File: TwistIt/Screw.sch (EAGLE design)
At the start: 7 parts

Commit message: Brush up twistit
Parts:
- removed U$3: (no value), pie:POGO_PIN
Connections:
- net PIN2 renamed P2
- removed net PIN1: R3.1, U$1.A0, U$2.P$2
- removed net PIN3: R1.1, U$1.A2, U$2.P$4
- new net P1: R1.1, U$1.A2, U$2.P$2
- new net P3: R3.1, U$1.A0, U$2.P$4
- net GND: now also U$2.P$5; no longer U$2.P$1
- net VCC: now also U$2.P$1; no longer U$2.P$5
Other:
- note removed: "PIN1"
- note removed: "PIN2"
- note removed: "PIN3"
- note removed: "Pin 1"
- note removed: "Pin 2"
- note removed: "Pin 3"
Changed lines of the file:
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@@
 <part name="R2" library="resistor" deviceset="R-US_" device="R0603"/>
 <part name="R3" library="resistor" deviceset="R-US_" device="R0603"/>
-<part name="SUPPLY1" library="pie" deviceset="GND" device=""/>
 <part name="SUPPLY2" library="pie" deviceset="GND" device=""/>
 <part name="JP1" library="jumper" deviceset="JP1E" device=""/>
 <part name="U$2" library="pie" deviceset="5PIN_SCREW" device=""/>
-<part name="U$3" library="pie" deviceset="POGO_PIN" device=""/>
+<part name="SUPPLY1" library="pie" deviceset="GND" device=""/>
 </parts>
 <sheets>
 <sheet>
 <plain>
-<text x="134.62" y="114.3" size="1.778" layer="91">Pin 1</text>
-<text x="127" y="114.3" size="1.778" layer="91">Pin 2</text>
-<text x="119.38" y="114.3" size="1.778" layer="91">Pin 3</text>
-<text x="83.82" y="88.9" size="1.778" layer="91">PIN1</text>
-<text x="83.82" y="91.44" size="1.778" layer="91">PIN2</text>
-<text x="83.82" y="93.98" size="1.778" layer="91">PIN3</text>
 </plain>
 <instances>
@@
 <instance part="R2" gate="G$1" x="116.84" y="99.06" rot="R180"/>
 <instance part="R3" gate="G$1" x="116.84" y="93.98" rot="R180"/>
-<instance part="SUPPLY1" gate="GND" x="134.62" y="81.28"/>
 <instance part="SUPPLY2" gate="GND" x="27.94" y="99.06"/>
 <instance part="JP1" gate="A" x="93.98" y="101.6"/>
-<instance part="U$2" gate="G$1" x="152.4" y="96.52"/>
-<instance part="U$3" gate="G$1" x="170.18" y="116.84"/>
+<instance part="U$2" gate="G$1" x="101.6" y="71.12" rot="R180"/>
+<instance part="SUPPLY1" gate="GND" x="124.46" y="55.88"/>
 </instances>
 <busses>
@@
 </segment>
 <segment>
-<wire x1="134.62" y1="88.9" x2="134.62" y2="83.82" width="0.1524" layer="91"/>
+<pinref part="U$2" gate="G$1" pin="P$5"/>
+<wire x1="116.84" y1="58.42" x2="124.46" y2="58.42" width="0.1524" layer="91"/>
 <pinref part="SUPPLY1" gate="GND" pin="GND"/>
-<pinref part="U$2" gate="G$1" pin="P$1"/>
-<wire x1="134.62" y1="88.9" x2="137.16" y2="88.9" width="0.1524" layer="91"/>
-<junction x="137.16" y="88.9"/>
+</segment>
+</net>
+<net name="P1" class="0">
+<segment>
+<pinref part="R1" gate="G$1" pin="1"/>
+<wire x1="121.92" y1="104.14" x2="129.54" y2="104.14" width="0.1524" layer="91"/>
+</segment>
+<segment>
+<pinref part="U$2" gate="G$1" pin="P$2"/>
+<wire x1="116.84" y1="73.66" x2="124.46" y2="73.66" width="0.1524" layer="91"/>
+<label x="121.92" y="73.66" size="1.778" layer="95"/>
+</segment>
+<segment>
+<pinref part="U$1" gate="G$1" pin="A2"/>
+<wire x1="76.2" y1="93.98" x2="83.82" y2="93.98" width="0.1524" layer="91"/>
 </segment>
 </net>
 <net name="VCC" class="0">
 <segment>
+<pinref part="U$2" gate="G$1" pin="P$1"/>
+<wire x1="116.84" y1="78.74" x2="124.46" y2="78.74" width="0.1524" layer="91"/>
+<label x="121.92" y="78.74" size="1.778" layer="95"/>
+</segment>
+<segment>
 <pinref part="JP1" gate="A" pin="1"/>
 <pinref part="U$1" gate="G$1" pin="VCC"/>
-<wire x1="76.2" y1="99.06" x2="86.36" y2="99.06" width="0.1524" layer="91"/>
-<wire x1="86.36" y1="99.06" x2="93.98" y2="99.06" width="0.1524" layer="91"/>
-<wire x1="86.36" y1="99.06" x2="86.36" y2="109.22" width="0.1524" layer="91"/>
-<junction x="86.36" y="99.06"/>
-<pinref part="U$2" gate="G$1" pin="P$5"/>
-<wire x1="86.36" y1="109.22" x2="137.16" y2="109.22" width="0.1524" layer="91"/>
-<junction x="137.16" y="109.22"/>
+<wire x1="76.2" y1="99.06" x2="93.98" y2="99.06" width="0.1524" layer="91"/>
 </segment>
 </net>
-<net name="PIN1" class="0">
+<net name="P2" class="0">
+<segment>
+<pinref part="U$2" gate="G$1" pin="P$3"/>
+<wire x1="116.84" y1="68.58" x2="124.46" y2="68.58" width="0.1524" layer="91"/>
+<label x="121.92" y="68.58" size="1.778" layer="95"/>
+</segment>
+<segment>
+<pinref part="U$1" gate="G$1" pin="A1"/>
+<wire x1="76.2" y1="91.44" x2="83.82" y2="91.44" width="0.1524" layer="91"/>
+</segment>
+<segment>
+<pinref part="R2" gate="G$1" pin="1"/>
+<wire x1="121.92" y1="99.06" x2="129.54" y2="99.06" width="0.1524" layer="91"/>
+</segment>
+</net>
+<net name="P3" class="0">
+<segment>
+<pinref part="U$2" gate="G$1" pin="P$4"/>
+<wire x1="116.84" y1="63.5" x2="124.46" y2="63.5" width="0.1524" layer="91"/>
+<label x="121.92" y="63.5" size="1.778" layer="95"/>
+</segment>
 <segment>
 <pinref part="U$1" gate="G$1" pin="A0"/>
@@
 <segment>
 <pinref part="R3" gate="G$1" pin="1"/>
-<wire x1="121.92" y1="93.98" x2="124.46" y2="93.98" width="0.1524" layer="91"/>
-<wire x1="124.46" y1="93.98" x2="124.46" y2="111.76" width="0.1524" layer="91"/>
-<pinref part="U$2" gate="G$1" pin="P$2"/>
-<wire x1="124.46" y1="93.98" x2="137.16" y2="93.98" width="0.1524" layer="91"/>
-<junction x="124.46" y="93.98"/>
-<junction x="137.16" y="93.98"/>
+<wire x1="121.92" y1="93.98" x2="129.54" y2="93.98" width="0.1524" layer="91"/>
 </segment>
 </net>
-<net name="PIN2" class="0">
-<segment>
-<pinref part="R2" gate="G$1" pin="1"/>
-<wire x1="121.92" y1="99.06" x2="129.54" y2="99.06" width="0.1524" layer="91"/>
-<wire x1="129.54" y1="99.06" x2="137.16" y2="99.06" width="0.1524" layer="91"/>
-<wire x1="137.16" y1="99.06" x2="138.43" y2="99.06" width="0.1524" layer="91"/>
-<wire x1="129.54" y1="99.06" x2="129.54" y2="111.76" width="0.1524" layer="91"/>
-<junction x="129.54" y="99.06"/>
-<pinref part="U$2" gate="G$1" pin="P$3"/>
-<junction x="137.16" y="99.06"/>
-</segment>
-<segment>
-<pinref part="U$1" gate="G$1" pin="A1"/>
-<wire x1="76.2" y1="91.44" x2="83.82" y2="91.44" width="0.1524" layer="91"/>
-</segment>
-</net>
-<net name="PIN3" class="0">
-<segment>
-<pinref part="U$1" gate="G$1" pin="A2"/>
-<wire x1="76.2" y1="93.98" x2="83.82" y2="93.98" width="0.1524" layer="91"/>
-</segment>
-<segment>
-<pinref part="R1" gate="G$1" pin="1"/>
-<wire x1="121.92" y1="104.14" x2="134.62" y2="104.14" width="0.1524" layer="91"/>
-<wire x1="134.62" y1="104.14" x2="137.16" y2="104.14" width="0.1524" layer="91"/>
-<wire x1="137.16" y1="104.14" x2="138.43" y2="104.14" width="0.1524" layer="91"/>
-<wire x1="134.62" y1="104.14" x2="134.62" y2="111.76" width="0.1524" layer="91"/>
-<junction x="134.62" y="104.14"/>
-<pinref part="U$2" gate="G$1" pin="P$4"/>
-<junction x="137.16" y="104.14"/>
-</segment>
-</net>

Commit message: Minor fixes everywhere
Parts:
- removed U$2: 5PIN_SCREW, pie:5PIN_SCREW
- added ST1: (no value), pie:5PIN_SCREW
- R1, R2, R3: value (none) -> 330
- renumbered U$1 to APM
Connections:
- net GND: now also ST1.P$5; no longer U$2.P$5
- net P1: now also ST1.P$2; no longer U$2.P$2
- net P2: now also ST1.P$3; no longer U$2.P$3
- net P3: now also ST1.P$4; no longer U$2.P$4
- net VCC: now also ST1.P$1; no longer U$2.P$1
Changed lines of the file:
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@@
 </classes>
 <parts>
-<part name="U$1" library="pie" deviceset="ARDUINO_PRO_MICRO" device=""/>
-<part name="FRAME1" library="pie" deviceset="FRAME-LETTER" device="">
-<attribute name="REVISION" value="A"/>
+<part name="APM" library="pie" deviceset="ARDUINO_PRO_MICRO" device=""/>
+<part name="FRAME1" library="pie" deviceset="FRAME_SCHEMATIC" device="">
+<attribute name="AUTHOR" value="Mohammed Hossain, Seiya Ono"/>
+<attribute name="REVISION" value="9B"/>
 </part>
-<part name="R1" library="resistor" deviceset="R-US_" device="R0603"/>
-<part name="R2" library="resistor" deviceset="R-US_" device="R0603"/>
-<part name="R3" library="resistor" deviceset="R-US_" device="R0603"/>
+<part name="R1" library="resistor" deviceset="R-US_" device="R0603" value="330"/>
+<part name="R2" library="resistor" deviceset="R-US_" device="R0603" value="330"/>
+<part name="R3" library="resistor" deviceset="R-US_" device="R0603" value="330"/>
 <part name="SUPPLY2" library="pie" deviceset="GND" device=""/>
 <part name="JP1" library="jumper" deviceset="JP1E" device=""/>
-<part name="U$2" library="pie" deviceset="5PIN_SCREW" device=""/>
+<part name="ST1" library="pie" deviceset="5PIN_SCREW" device=""/>
 <part name="SUPPLY1" library="pie" deviceset="GND" device=""/>
 </parts>
@@
 </plain>
 <instances>
-<instance part="U$1" gate="G$1" x="60.96" y="93.98"/>
-<instance part="FRAME1" gate="G$1" x="0" y="0"/>
+<instance part="APM" gate="G$1" x="60.96" y="93.98"/>
+<instance part="FRAME1" gate="G$1" x="0" y="0">
+<attribute name="AUTHOR" x="0" y="0" size="1.778" layer="96" display="off"/>
+</instance>
 <instance part="FRAME1" gate="G$2" x="147.32" y="0">
 <attribute name="REVISION" x="147.32" y="0" size="1.778" layer="96"/>
@@
 <instance part="SUPPLY2" gate="GND" x="27.94" y="99.06"/>
 <instance part="JP1" gate="A" x="93.98" y="101.6"/>
-<instance part="U$2" gate="G$1" x="101.6" y="71.12" rot="R180"/>
+<instance part="ST1" gate="G$1" x="154.94" y="68.58"/>
 <instance part="SUPPLY1" gate="GND" x="124.46" y="55.88"/>
 </instances>
@@
 <segment>
 <pinref part="SUPPLY2" gate="GND" pin="GND"/>
-<pinref part="U$1" gate="G$1" pin="GND@0"/>
+<pinref part="APM" gate="G$1" pin="GND@0"/>
 <wire x1="27.94" y1="101.6" x2="48.26" y2="101.6" width="0.1524" layer="91"/>
 </segment>
 <segment>
-<pinref part="U$2" gate="G$1" pin="P$5"/>
-<wire x1="116.84" y1="58.42" x2="124.46" y2="58.42" width="0.1524" layer="91"/>
+<pinref part="ST1" gate="G$1" pin="P$5"/>
+<wire x1="134.62" y1="58.42" x2="124.46" y2="58.42" width="0.1524" layer="91"/>
 <pinref part="SUPPLY1" gate="GND" pin="GND"/>
 </segment>
@@
 </segment>
 <segment>
-<pinref part="U$2" gate="G$1" pin="P$2"/>
-<wire x1="116.84" y1="73.66" x2="124.46" y2="73.66" width="0.1524" layer="91"/>
+<pinref part="ST1" gate="G$1" pin="P$2"/>
+<wire x1="134.62" y1="73.66" x2="124.46" y2="73.66" width="0.1524" layer="91"/>
 <label x="121.92" y="73.66" size="1.778" layer="95"/>
 </segment>
 <segment>
-<pinref part="U$1" gate="G$1" pin="A2"/>
+<pinref part="APM" gate="G$1" pin="A2"/>
 <wire x1="76.2" y1="93.98" x2="83.82" y2="93.98" width="0.1524" layer="91"/>
 </segment>
@@
 <net name="VCC" class="0">
 <segment>
-<pinref part="U$2" gate="G$1" pin="P$1"/>
-<wire x1="116.84" y1="78.74" x2="124.46" y2="78.74" width="0.1524" layer="91"/>
+<pinref part="ST1" gate="G$1" pin="P$1"/>
+<wire x1="134.62" y1="78.74" x2="124.46" y2="78.74" width="0.1524" layer="91"/>
 <label x="121.92" y="78.74" size="1.778" layer="95"/>
 </segment>
 <segment>
 <pinref part="JP1" gate="A" pin="1"/>
-<pinref part="U$1" gate="G$1" pin="VCC"/>
+<pinref part="APM" gate="G$1" pin="VCC"/>
 <wire x1="76.2" y1="99.06" x2="93.98" y2="99.06" width="0.1524" layer="91"/>
 </segment>
@@
 <net name="P2" class="0">
 <segment>
-<pinref part="U$2" gate="G$1" pin="P$3"/>
-<wire x1="116.84" y1="68.58" x2="124.46" y2="68.58" width="0.1524" layer="91"/>
+<pinref part="ST1" gate="G$1" pin="P$3"/>
+<wire x1="134.62" y1="68.58" x2="124.46" y2="68.58" width="0.1524" layer="91"/>
 <label x="121.92" y="68.58" size="1.778" layer="95"/>
 </segment>
 <segment>
-<pinref part="U$1" gate="G$1" pin="A1"/>
+<pinref part="APM" gate="G$1" pin="A1"/>
 <wire x1="76.2" y1="91.44" x2="83.82" y2="91.44" width="0.1524" layer="91"/>
 </segment>
@@
 <net name="P3" class="0">
 <segment>
-<pinref part="U$2" gate="G$1" pin="P$4"/>
-<wire x1="116.84" y1="63.5" x2="124.46" y2="63.5" width="0.1524" layer="91"/>
+<pinref part="ST1" gate="G$1" pin="P$4"/>
+<wire x1="134.62" y1="63.5" x2="124.46" y2="63.5" width="0.1524" layer="91"/>
 <label x="121.92" y="63.5" size="1.778" layer="95"/>
 </segment>
 <segment>
-<pinref part="U$1" gate="G$1" pin="A0"/>
+<pinref part="APM" gate="G$1" pin="A0"/>
 <wire x1="76.2" y1="88.9" x2="83.82" y2="88.9" width="0.1524" layer="91"/>
 </segment>

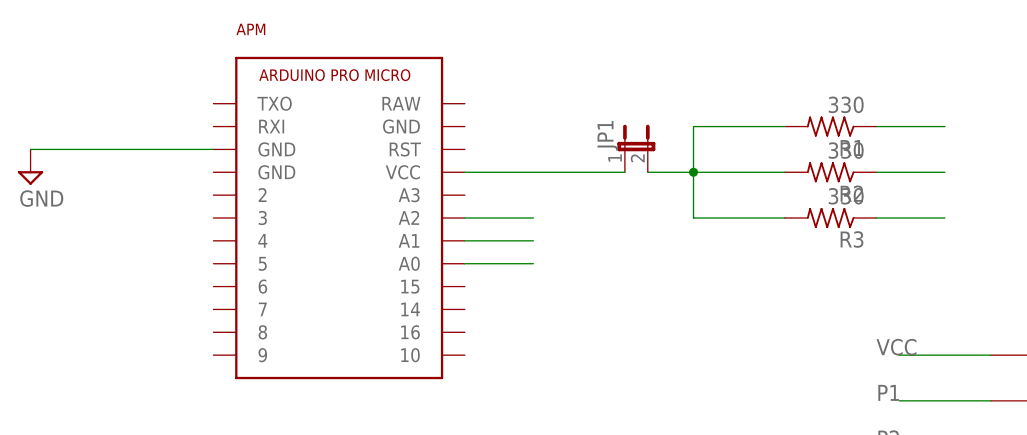
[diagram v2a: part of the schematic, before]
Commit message: Add screw terminals and names; change orientation to be ergonomic
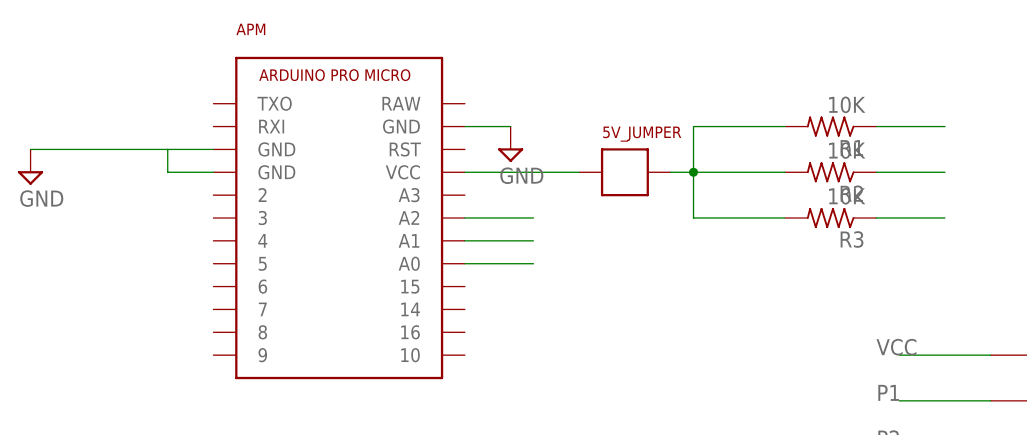
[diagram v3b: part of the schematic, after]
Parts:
- removed JP1: (no value), jumper:JP1E
- added 5V_JUMPER: JUMPER, pie:JUMPER
- R1, R2, R3: value 330 -> 10K
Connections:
- net 5V: now also 5V_JUMPER.P$2; no longer JP1.2
- net GND: now also APM.GND@1, APM.GND@2
- net VCC: now also 5V_JUMPER.P$1; no longer JP1.1
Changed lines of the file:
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@@
 <attribute name="REVISION" value="9B"/>
 </part>
-<part name="R1" library="resistor" deviceset="R-US_" device="R0603" value="330"/>
-<part name="R2" library="resistor" deviceset="R-US_" device="R0603" value="330"/>
-<part name="R3" library="resistor" deviceset="R-US_" device="R0603" value="330"/>
+<part name="R1" library="resistor" deviceset="R-US_" device="R0603" value="10K"/>
+<part name="R2" library="resistor" deviceset="R-US_" device="R0603" value="10K"/>
+<part name="R3" library="resistor" deviceset="R-US_" device="R0603" value="10K"/>
 <part name="SUPPLY2" library="pie" deviceset="GND" device=""/>
-<part name="JP1" library="jumper" deviceset="JP1E" device=""/>
 <part name="ST1" library="pie" deviceset="5PIN_SCREW" device=""/>
 <part name="SUPPLY1" library="pie" deviceset="GND" device=""/>
+<part name="SUPPLY3" library="pie" deviceset="GND" device=""/>
+<part name="5V_JUMPER" library="pie" deviceset="JUMPER" device=""/>
 </parts>
 <sheets>
@@
 <instance part="R3" gate="G$1" x="116.84" y="93.98" rot="R180"/>
 <instance part="SUPPLY2" gate="GND" x="27.94" y="99.06"/>
-<instance part="JP1" gate="A" x="93.98" y="101.6"/>
 <instance part="ST1" gate="G$1" x="154.94" y="68.58"/>
 <instance part="SUPPLY1" gate="GND" x="124.46" y="55.88"/>
+<instance part="SUPPLY3" gate="GND" x="81.28" y="101.6"/>
+<instance part="5V_JUMPER" gate="G$1" x="93.98" y="99.06"/>
 </instances>
 <busses>
@@
 <wire x1="111.76" y1="104.14" x2="101.6" y2="104.14" width="0.1524" layer="91"/>
 <wire x1="101.6" y1="104.14" x2="101.6" y2="99.06" width="0.1524" layer="91"/>
-<pinref part="JP1" gate="A" pin="2"/>
-<wire x1="96.52" y1="99.06" x2="101.6" y2="99.06" width="0.1524" layer="91"/>
+<wire x1="99.06" y1="99.06" x2="101.6" y2="99.06" width="0.1524" layer="91"/>
+<pinref part="5V_JUMPER" gate="G$1" pin="P$2"/>
 </segment>
 </net>
@@
 <pinref part="SUPPLY2" gate="GND" pin="GND"/>
 <pinref part="APM" gate="G$1" pin="GND@0"/>
-<wire x1="27.94" y1="101.6" x2="48.26" y2="101.6" width="0.1524" layer="91"/>
+<wire x1="27.94" y1="101.6" x2="43.18" y2="101.6" width="0.1524" layer="91"/>
+<pinref part="APM" gate="G$1" pin="GND@1"/>
+<wire x1="43.18" y1="101.6" x2="48.26" y2="101.6" width="0.1524" layer="91"/>
+<wire x1="43.18" y1="101.6" x2="43.18" y2="99.06" width="0.1524" layer="91"/>
+<wire x1="43.18" y1="99.06" x2="48.26" y2="99.06" width="0.1524" layer="91"/>
 </segment>
 <segment>
@@
 <wire x1="134.62" y1="58.42" x2="124.46" y2="58.42" width="0.1524" layer="91"/>
 <pinref part="SUPPLY1" gate="GND" pin="GND"/>
+</segment>
+<segment>
+<pinref part="SUPPLY3" gate="GND" pin="GND"/>
+<pinref part="APM" gate="G$1" pin="GND@2"/>
+<wire x1="81.28" y1="104.14" x2="76.2" y2="104.14" width="0.1524" layer="91"/>
 </segment>
 </net>
@@
 </segment>
 <segment>
-<pinref part="JP1" gate="A" pin="1"/>
 <pinref part="APM" gate="G$1" pin="VCC"/>
-<wire x1="76.2" y1="99.06" x2="93.98" y2="99.06" width="0.1524" layer="91"/>
+<wire x1="76.2" y1="99.06" x2="88.9" y2="99.06" width="0.1524" layer="91"/>
+<pinref part="5V_JUMPER" gate="G$1" pin="P$1"/>
 </segment>
 </net>
